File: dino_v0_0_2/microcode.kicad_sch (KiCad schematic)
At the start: 8 parts, among them U15 AT28C64B, U16 74LS244N, U17 74LS244N, U9 AT28C64B

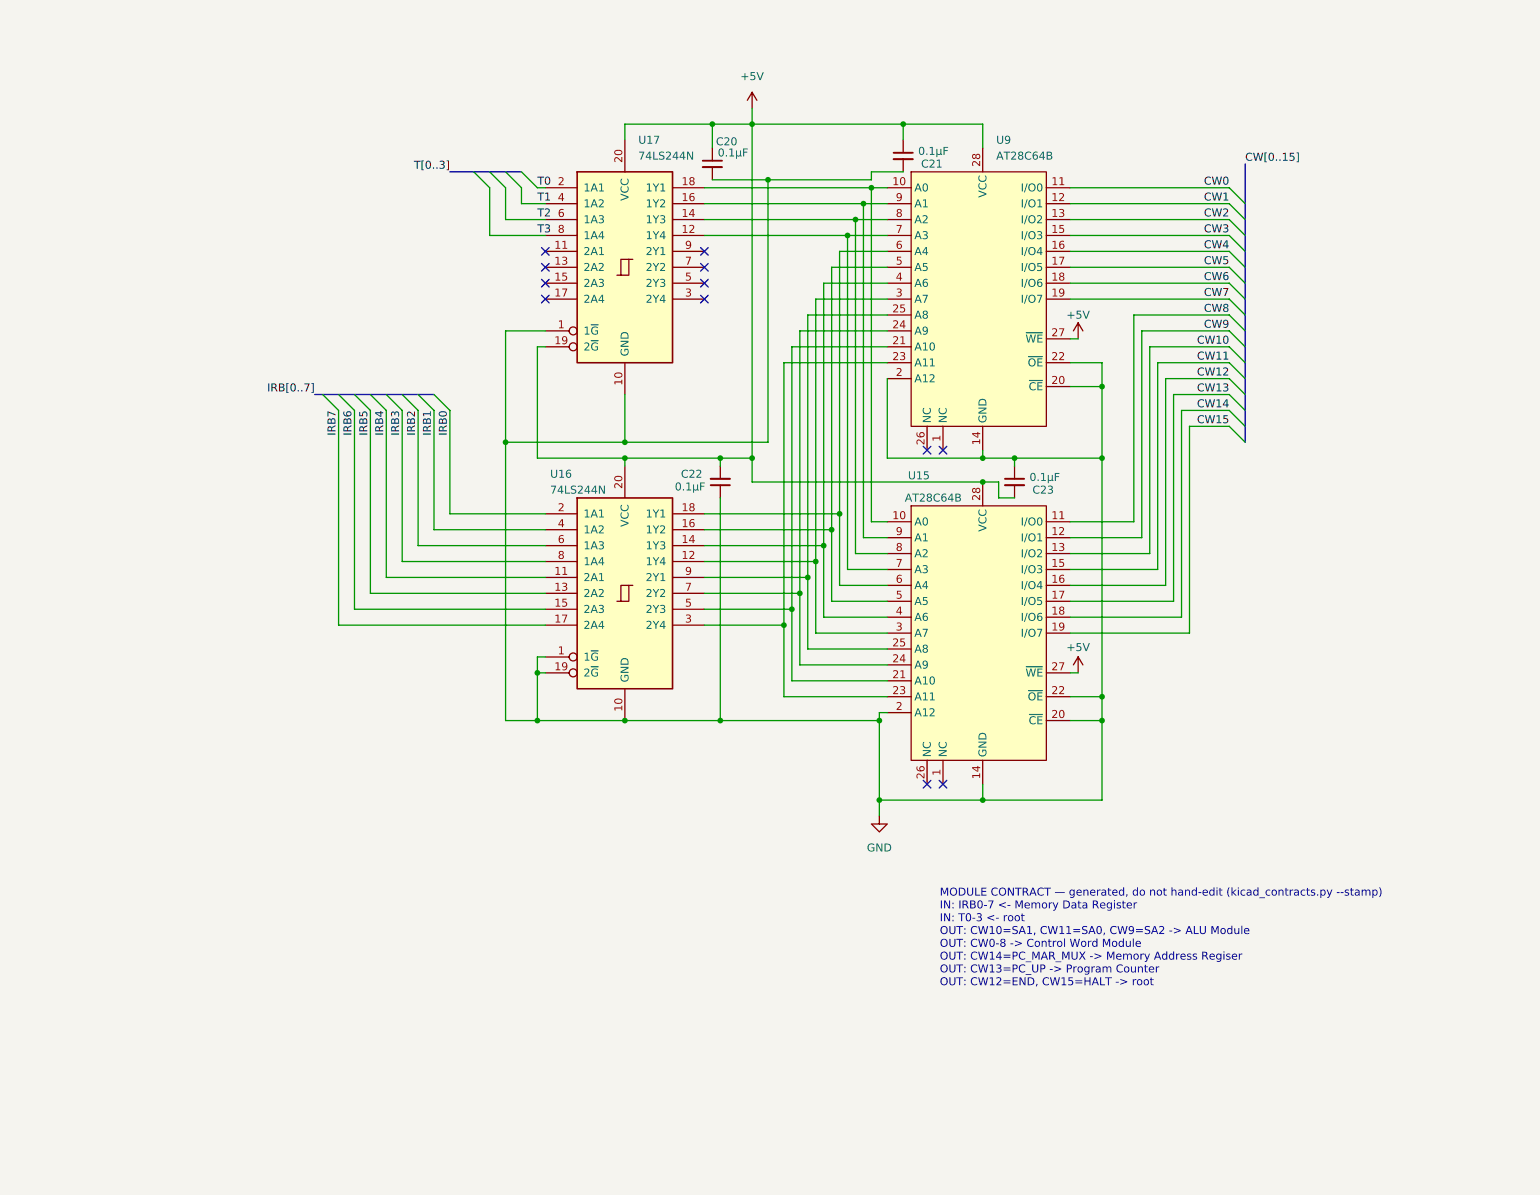
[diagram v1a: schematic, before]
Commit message: Stack pointer + third microcode EEPROM: schematic, tooling, and ISA
Twelve chips, four sheets, seven instructions. The whole stack executes on
the gate model; the rig is detached so nothing has run on real hardware.

  U23         AT28C64B   third microcode EEPROM, CW16-23     microcode
  U70 / U71   '138       SRC / DST bank-1 decoders           control_word
  U63-U66     '169       16-bit stack pointer                stack_pointer
  U67 / U68   '245       SP hi/lo readback -> MDR            stack_pointer
  U69         '08        ~{SP_CE} = AND(~SP_UP, ~SP_DOWN)    stack_pointer
  U72 / U73   '245       PC0-7 / PC8-15 -> MDR               mdr

  LXISP 0x14   CALL 0x33   RET 0x34
  PUSHA 0x61   POPA 0x62   PUSHB 0x63   POPB 0x64

THE CONTROL WORD IS 24 BITS. Every new bit is polarised so 0xFF -- an erased
AT28C64B -- is today's machine, the same reasoning that made HALT=0xFF. Only
~{SRC_BANK} and ~{DST_BANK} are wired; ~{CIN_SEL}, ~{MISC_BANK},
~{ADDR_SEL1}, FLAG_SEL0/1 and FLAG_POL are burned into all 4096 rows and
wired to nothing, so no reburn is needed when their decode arrives.

Bank switching costs zero inverters: E3 is active-high and E1 active-low, so
bank 0 hangs off E3 and bank 1 off E1 of the same bit. SRC/DST codes 8-15 are
bank 1; word() derives the bank bit FROM the code, so a caller cannot select
SP_LO and forget to switch banks.

MISC IS NOW FULL. U29's O5/O7 were the last two free codes and the stack
spends both. O0 is the NONE slot and can never be reclaimed.

Deviations from dino_hardware_growth_plan.md, corrected inline there:

  - SRC3/DST3/MISC3 -> ~{SRC_BANK}/~{DST_BANK}/~{MISC_BANK}. A '138 has three
    address pins; the new bit is an ENABLE, not a fourth.
  - COND[2:0] -> FLAG_SEL0/FLAG_SEL1/FLAG_POL. COND0 loses KiCad's alias sort
    to CW21, steals the net off the CW bus, and produces net_not_bus_member.
  - CIN is a SELECT, not a carry value: one ROM bit cannot BE the carry.
  - MISC had two free codes, not three, and SP_LOAD is a DST d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
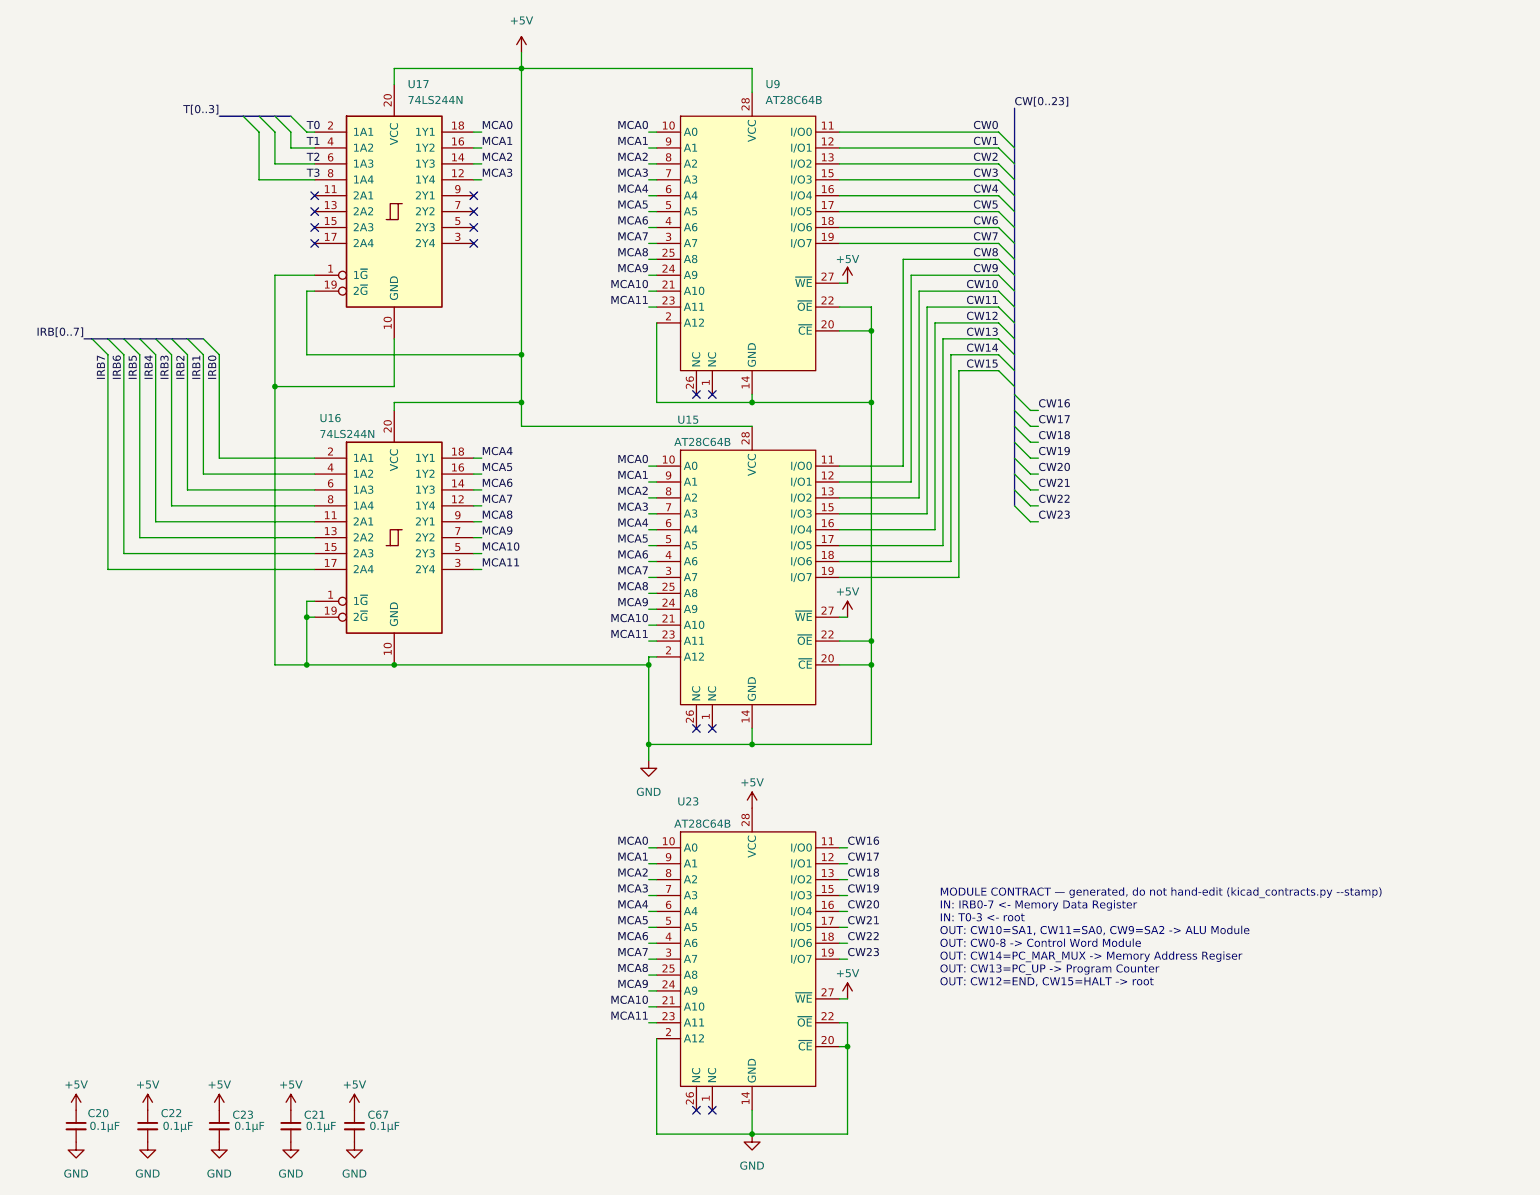
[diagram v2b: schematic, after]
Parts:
- added C67: 0.1µF, symbol Device:C_Small
- added U23: AT28C64B, symbol Memory_EEPROM:AT28C64B
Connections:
- net +5V: now also C22.1, C23.1, C67.1, U23.27 (~{WE}), U23.28 (VCC); no longer C22.2, C23.2
- net GND: now also C22.2, C23.2, C67.2, U23.14 (GND), U23.2 (A12), U23.20 (~{CE}), U23.22 (~{OE}); no longer C22.1, C23.1
- net MCA0: now reaches U15.10 (A0), U17.18 (1Y1), U9.10 (A0)
- net MCA0: now also U23.10 (A0)
- net MCA10: now reaches U15.21 (A10), U16.5 (2Y3), U9.21 (A10)
- net MCA10: now also U23.21 (A10)
- net MCA11: now reaches U15.23 (A11), U16.3 (2Y4), U9.23 (A11)
- net MCA11: now also U23.23 (A11)
- net MCA9: now reaches U15.24 (A9), U16.7 (2Y2), U9.24 (A9)
- net MCA9: now also U23.24 (A9)
- net MCA8: now reaches U15.25 (A8), U16.9 (2Y1), U9.25 (A8)
- net MCA8: now also U23.25 (A8)
- net MCA7: now reaches U15.3 (A7), U16.12 (1Y4), U9.3 (A7)
- net MCA7: now also U23.3 (A7)
- net MCA6: now reaches U15.4 (A6), U16.14 (1Y3), U9.4 (A6)
- net MCA6: now also U23.4 (A6)
- net MCA5: now reaches U15.5 (A5), U16.16 (1Y2), U9.5 (A5)
- net MCA5: now also U23.5 (A5)
- net MCA4: now reaches U15.6 (A4), U16.18 (1Y1), U9.6 (A4)
- net MCA4: now also U23.6 (A4)
- net MCA3: now reaches U15.7 (A3), U17.12 (1Y4), U9.7 (A3)
- net MCA3: now also U23.7 (A3)
- net MCA2: now reaches U15.8 (A2), U17.14 (1Y3), U9.8 (A2)
- net MCA2: now also U23.8 (A2)
- net MCA1: now reaches U15.9 (A1), U17.16 (1Y2), U9.9 (A1)
- net MCA1: now also U23.9 (A1)
- new net CW16: U23.11 (I/O0)
- new net CW17: U23.12 (I/O1)
- new net CW18: U23.13 (I/O2)
- new net CW19: U23.15 (I/O3)
- new net CW20: U23.16 (I/O4)
- new net CW21: U23.17 (I/O5)
- new net CW22: U23.18 (I/O6)
- new net CW23: U23.19 (I/O7)
- no-connect marks 12 -> 14
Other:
- moved on the sheet: C20, C21, C22, C23, U15, U16, U17, U9

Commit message: fix(schematic): declare matching label sets so aliased nets stay one net
Three board-to-board wires were absent from the generated continuity
checklist, which is the only coverage the netlist->copper step has. A wire
missing from that list is driven by no test and sampled by no test -- the
MAR-lo post-mortem in one sentence.

Cause: cross-sheet connectivity in this design is a naming convention (all
labels are sheet-local; KiCad joins nothing between sheets). kicad_netlist
keys a net on its full label set, joined. When one sheet carries an alias and
another doesn't, the same physical wire gets two keys, both look single-sheet,
and continuity_checklist's cross-sheet filter drops the whole net.

    M15/ROM_EN   mar had both labels, memory had only ROM_EN (on a stub that
                 never joined U24.20's wire), program_counter had only M15.
                 The ROM chip-enable. Missing from every checklist ever
                 generated; survived only because a dead ~CE means the machine
                 never boots, so it self-reports.
    CW17 / CW18  microcode had the bare names, control_word had both. These
                 are U23's only wired outputs -- the entire bank-1 feature
                 rides on them, and both decoders lose their enable if either
                 is unlanded, which at the bench reads like a bad ROM burn.

Fix is in the schematic, not the tool: every sheet touching an aliased net now
declares the same label set. Alias ordering already satisfied the CWnn rule
(`~` sorts after `C`), so CW17/CW18 stay canonical and stay bus members.

  memory           U24.20  ROM_EN -> M15/ROM_EN
  program_counter  U12.9   M15    -> M15/ROM_EN
                   U14.9   M15    -> M15/ROM_EN
  microcode        U23.12  CW17   -> CW17/~{SRC_BANK}
                   U23.13  CW18   -> CW18/~{DST_BANK}

stack_pointer.kicad_sch is UUID churn only, zero connectivity change: the
sheet shipped with 14 duplicate UUIDs (one repeated 5x, consistent with the
four 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
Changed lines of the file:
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@@
 	(wire
 		(pts
-			(xy 143.51 151.13) (xy 144.78 151.13)
+			(xy 143.51 151.13) (xy 152.4 151.13)
 		)
 		(stroke
@@
 	(wire
 		(pts
-			(xy 143.51 153.67) (xy 144.78 153.67)
+			(xy 143.51 153.67) (xy 153.67 153.67)
 		)
 		(stroke
@@
 		)
 	)
+	(label "~{DST_BANK}"
+		(at 153.67 153.67 0)
+		(effects
+			(font
+				(size 1.27 1.27)
+			)
+			(justify left bottom)
+		)
+	)
 	(label "IRB0"
 		(at 44.45 69.85 270)
@@
 		(effects
 			(font
+				(size 1.27 1.27)
+			)
+			(justify left bottom)
+		)
+	)
+	(label "~{SRC_BANK}"
+		(at 152.4 151.13 0)
+		(effects
+			(font

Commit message: schematic: join five aliased nets, and ledger the root-sheet gap
FIVE LIVE WIRES WERE IN THE CHECKLIST'S NO-CONNECT BUCKET, under the
heading "nothing to land and nothing to beep against."

  CW9/SA2           U15.12  <->  U38.7, U40.7
  CW10/SA1          U15.13  <->  U38.6, U40.6, U53.12
  CW11/SA0          U15.15  <->  U38.5, U40.5, U53.13
  CW13/PC_UP        U15.17  <->  U36.1
  CW14/PC_MAR_MUX   U15.18  <->  U54.19, U59.19, U60.11, U60.12

The microcode sheet labelled each net CWnn; the consumer sheet labelled it
SA2 / PC_UP / PC_MAR_MUX. Two label sets, two net keys, both look
sheet-local, and the cross-sheet filter drops the wire -- the M15/ROM_EN
failure, five more times.

alias_splits() could not see it. It keys on a shared BASE label, which is
how it catches CW17 vs CW17/~{SRC_BANK}. CW9 and SA2 share no substring,
so the guard was structurally blind to this shape.

Applied via kicad_gen_sheet.py ops files -- deterministic uuid5, applied
markers, valid s-expression splices -- not hand edits. Every touched sheet
reparses. dino_sheet_contracts.md is UNCHANGED, which confirms the
contracts path (hierarchical sheet pins) was always right and only the
checklist path was blind. unlanded_stubs 20 -> 14; the five now emit as
NEW: with beep partners.

Cosmetic: CW13 on program_counter sits at the same coordinate as PC_UP.
That anchor has no horizontal run, and same-point is the only placement
guaranteed to attach to the right node. Drag apart in KiCad when convenient.

A THIRD BLIND SPOT, FOUND AND LEDGERED RATHER THAN FIXED. net_pins()
walks the ten child sheets and NOT the root sheet:

    alu control_word input_output mar mdr memory microcode
    program_counter registers_a_b stack_pointer      -- no root

Root carries U6 (T-counter), U7/U8 (T decoders), U20 (divider), U27
(clock/reset), U56, U61, Y1, SW2 -- real parts on no child sheet. Their
pins can never reach a continuity checklist, and any child-sheet net
terminating on root is misreported as a no-connect. 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
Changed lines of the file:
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@@
 	(title_block
 		(title "Dino v0.0.3")
-		(date "2026-07-12")
-		(rev "v1.2.0")
+		(date "2026-08-23")
+		(rev "v1.3.0")
 		(comment 1 "The Microcode Decoder Module")
-		(comment 3 "An 8-bit computer with 16-bit addressing and 16-bit control words")
+		(comment 3 "An 8-bit computer with 16-bit addressing and 24-bit control words")
 		(comment 4 "A Turing-Complete 8-bit \"Computer\"")
 	)
@@
 		)
 	)
+	(label "SA2"
+		(at 165.1 57.15 180)
+		(effects
+			(font
+				(size 1.27 1.27)
+			)
+			(justify right bottom)
+		)
+	)
+	(label "SA1"
+		(at 165.1 59.69 180)
+		(effects
+			(font
+				(size 1.27 1.27)
+			)
+			(justify right bottom)
+		)
+	)
+	(label "SA0"
+		(at 165.1 62.23 180)
+		(effects
+			(font
+				(size 1.27 1.27)
+			)
+			(justify right bottom)
+		)
+	)
+	(label "PC_UP"
+		(at 165.1 67.31 180)
+		(effects
+			(font
+				(size 1.27 1.27)
+			)
+			(justify right bottom)
+		)
+	)
+	(label "PC_MAR_MUX"
+		(at 165.1 69.85 180)
+		(effects
+			(font
+				(size 1.27 1.27)
+			)
+			(justify right bottom)
+		)
+	)
